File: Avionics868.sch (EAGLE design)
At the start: 63 parts, among them SW1 SPST_TACT-KMR2, U1 ATSAMD21G18_QFN, U2 SPX3819M5-L-3-0, U3 MCP73831T-2ACI/OT, U4 MPU-9250, U5 SIM868, U6 BMP180, X1 JSTPH, X2 32.768, X3 microUSB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

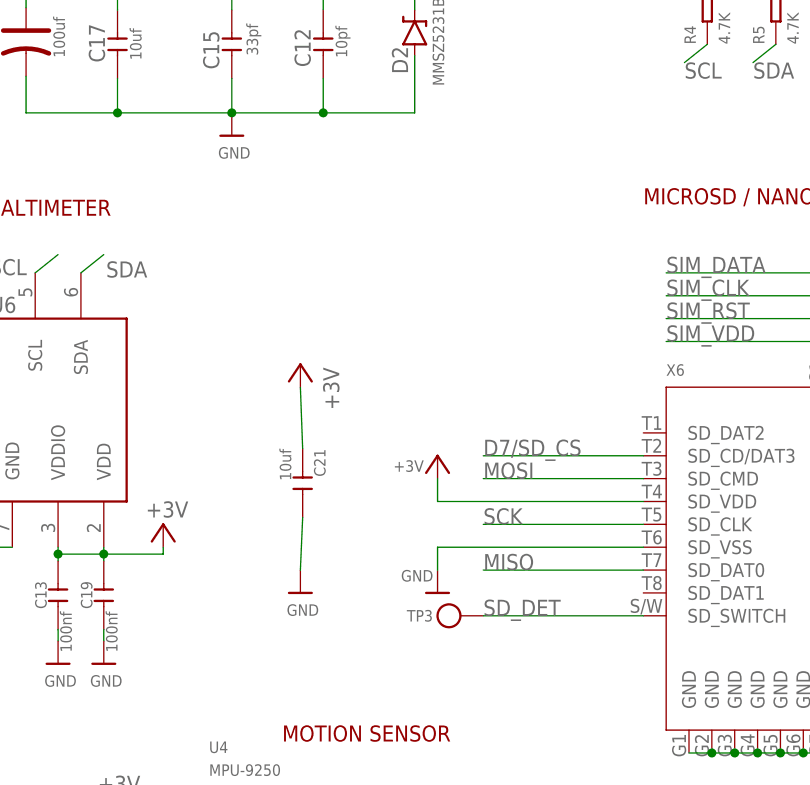
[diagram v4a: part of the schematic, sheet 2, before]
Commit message: More bypass for SIM and SD
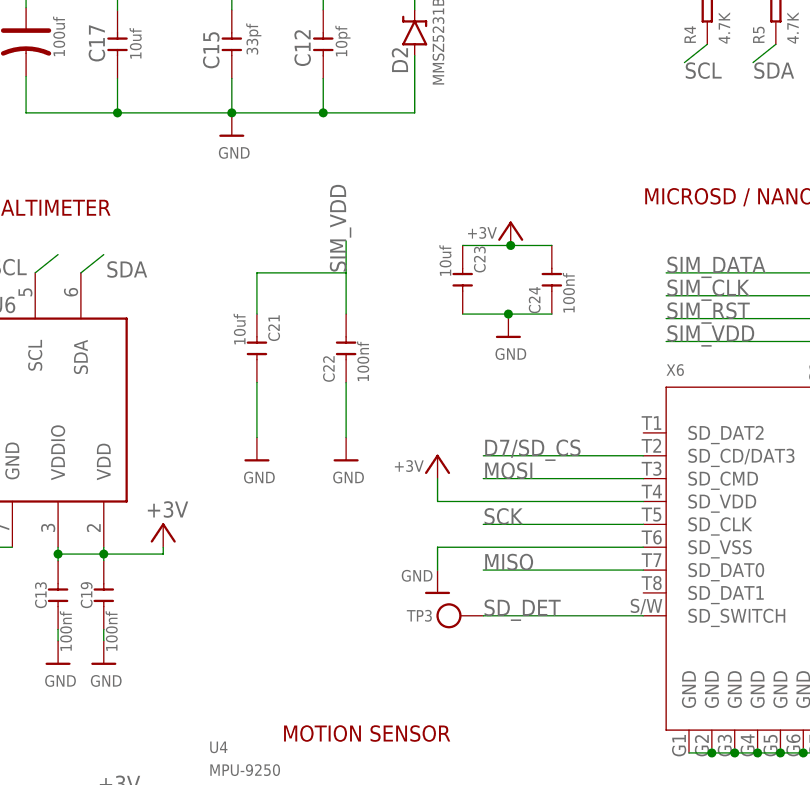
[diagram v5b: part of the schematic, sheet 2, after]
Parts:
- removed U$35: FIDUCIAL"", microbuilder:FIDUCIAL""
- added C22, C24: 100nf, Seeed-Capacitor-2016:CERAMIC-100NF-25V-10%-X7R(0402)
- added C23: 10uf, Seeed-Capacitor-2016:CERAMIC-10UF-10V-10%-X5R(0603)
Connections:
- net +3V: now also C23.1, C24.2; no longer C21.1
- net GND: now also C22.1, C23.2, C24.1
- net SIM_VDD: now also C21.1, C22.2
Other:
- moved on the sheet: C21
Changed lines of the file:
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@@
 <part name="GND10" library="supply1" deviceset="GND" device=""/>
 <part name="U$34" library="microbuilder" deviceset="FIDUCIAL" device="&quot;&quot;"/>
-<part name="U$35" library="microbuilder" deviceset="FIDUCIAL" device="&quot;&quot;"/>
 <part name="SW1" library="adafruit" deviceset="SPST_TACT" device="-KMR2"/>
 <part name="U$31" library="microbuilder" deviceset="MOUNTINGHOLE" device="2.5"/>
@@
 <part name="U$45" library="microbuilder" deviceset="GND" device=""/>
 <part name="C21" library="Seeed-Capacitor-2016" deviceset="CERAMIC-10UF-10V-10%-X5R(0603)" device="" value="10uf"/>
+<part name="U$49" library="microbuilder" deviceset="GND" device=""/>
+<part name="C22" library="Seeed-Capacitor-2016" deviceset="CERAMIC-100NF-25V-10%-X7R(0402)" device="" value="100nf"/>
+<part name="U$50" library="microbuilder" deviceset="GND" device=""/>
+<part name="C23" library="Seeed-Capacitor-2016" deviceset="CERAMIC-10UF-10V-10%-X5R(0603)" device="" value="10uf"/>
+<part name="C24" library="Seeed-Capacitor-2016" deviceset="CERAMIC-100NF-25V-10%-X7R(0402)" device="" value="100nf"/>
 <part name="+3V14" library="Custom" deviceset="+3V" device=""/>
-<part name="U$49" library="microbuilder" deviceset="GND" device=""/>
+<part name="U$35" library="microbuilder" deviceset="GND" device=""/>
 </parts>
 <sheets>
@@
 <instance part="GND10" gate="1" x="246.38" y="43.18" rot="MR0"/>
 <instance part="U$34" gate="G$1" x="210.82" y="17.78"/>
-<instance part="U$35" gate="G$1" x="205.74" y="17.78"/>
 <instance part="SW1" gate="G$1" x="124.46" y="152.4" smashed="yes" rot="R270">
 <attribute name="NAME" x="121.92" y="158.75" size="1.778" layer="95"/>
@@
 <instance part="+3V5" gate="G$1" x="15.24" y="78.74" rot="MR0"/>
 <instance part="U$45" gate="G$1" x="15.24" y="53.34"/>
-<instance part="C21" gate="G$1" x="53.594" y="98.552" rot="R270"/>
-<instance part="+3V14" gate="G$1" x="53.34" y="111.76" rot="MR0"/>
-<instance part="U$49" gate="G$1" x="53.34" y="86.36"/>
+<instance part="C21" gate="G$1" x="48.514" y="113.538" rot="R270"/>
+<instance part="U$49" gate="G$1" x="48.514" y="101.092"/>
+<instance part="C22" gate="G$1" x="58.42" y="113.538" rot="R90"/>
+<instance part="U$50" gate="G$1" x="58.42" y="101.092"/>
+<instance part="C23" gate="G$1" x="71.374" y="121.158" rot="R270"/>
+<instance part="C24" gate="G$1" x="81.28" y="121.158" rot="R90"/>
+<instance part="+3V14" gate="G$1" x="76.708" y="127.508" smashed="yes" rot="MR0">
+<attribute name="VALUE" x="75.184" y="125.73" size="1.27" layer="96" rot="MR0"/>
+</instance>
+<instance part="U$35" gate="G$1" x="76.454" y="114.808"/>
 </instances>
 <busses>
@@
 <pinref part="C21" gate="G$1" pin="2"/>
 <pinref part="U$49" gate="G$1" pin="GND"/>
-<wire x1="53.34" y1="88.9" x2="53.594" y2="94.742" width="0.1524" layer="91"/>
+<wire x1="48.514" y1="103.632" x2="48.514" y2="109.728" width="0.1524" layer="91"/>
+</segment>
+<segment>
+<pinref part="C22" gate="G$1" pin="1"/>
+<pinref part="U$50" gate="G$1" pin="GND"/>
+<wire x1="58.42" y1="103.632" x2="58.42" y2="109.728" width="0.1524" layer="91"/>
+</segment>
+<segment>
+<pinref part="C24" gate="G$1" pin="1"/>
+<pinref part="C23" gate="G$1" pin="2"/>
+<wire x1="81.28" y1="117.348" x2="76.454" y2="117.348" width="0.1524" layer="91"/>
+<pinref part="U$35" gate="G$1" pin="GND"/>
+<wire x1="76.454" y1="117.348" x2="71.374" y2="117.348" width="0.1524" layer="91"/>
+<junction x="76.454" y="117.348"/>
 </segment>
 </net>
@@
 </segment>
 <segment>
-<pinref part="C21" gate="G$1" pin="1"/>
+<pinref part="C23" gate="G$1" pin="1"/>
+<pinref part="C24" gate="G$1" pin="2"/>
+<wire x1="71.374" y1="124.968" x2="76.708" y2="124.968" width="0.1524" layer="91"/>
 <pinref part="+3V14" gate="G$1" pin="+3V"/>
-<wire x1="53.594" y1="102.362" x2="53.34" y2="109.22" width="0.1524" layer="91"/>
+<wire x1="76.708" y1="124.968" x2="81.28" y2="124.968" width="0.1524" layer="91"/>
+<junction x="76.708" y="124.968"/>
 </segment>
 </net>
@@
 <label x="93.98" y="114.3" size="1.778" layer="95"/>
 </segment>
-</net>
+<segment>
+<pinref part="C22" gate="G$1" pin="2"/>
+<wire x1="58.42" y1="117.348" x2="58.42" y2="121.92" width="0.1524" layer="91"/>
+<label x="58.42" y="121.92" size="1.778" layer="95" rot="R90"/>
+<pinref part="C21" gate="G$1" pin="1"/>
+<wire x1="58.42" y1="121.92" x2="58.42" y2="125.476" width="0.1524" layer="91"/>
+<wire x1="48.514" y1="117.348" x2="48.514" y2="121.92" width="0.1524" layer="91"/>
+<wire x1="58.42" y1="121.92" x2="48.514" y2="121.92" width="0.1524" layer="91"/>
+</segment>
+</net>
